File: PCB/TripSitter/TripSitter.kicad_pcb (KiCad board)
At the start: 4 copper layers, 203 x 85 mm, 165 parts, among them IC1 MT25QL256ABA1EW9-0SIT, IC701 IP4220CZ6, J2 DE15_Plug_HighDensity_Mountin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, J201 Conn_ARM_JTAG_SWD_20, J3 USB_B_Micro, J4 Conn_02x07_Odd_Even, J6 EFM32_PinHeader_PortE, J7 HDMI_A_1.4, J801 Conn_02x05_Odd_Even, J802 Jack-DC, J803 USB_B_Micro, SW1 SW_Push_Open, SW801 SW_DPDT_x2, U1 XC7A100T-FGG484, U2 TPS54325_PWP_14, U201 EFM32GG11B420F2048GQ100, U202 IS62WVS2568FBLL-20NLI, U4 DSC1001DL5-100.0000T, U5 TPS54294PWP, U501 IS62WVS2568FBLL-20NLI, U502 IS62WVS2568FBLL-20NLI, U6 IS62WVS2568FBLL-20NLI, U7 TPD12S520DBT, Y201 48MHz

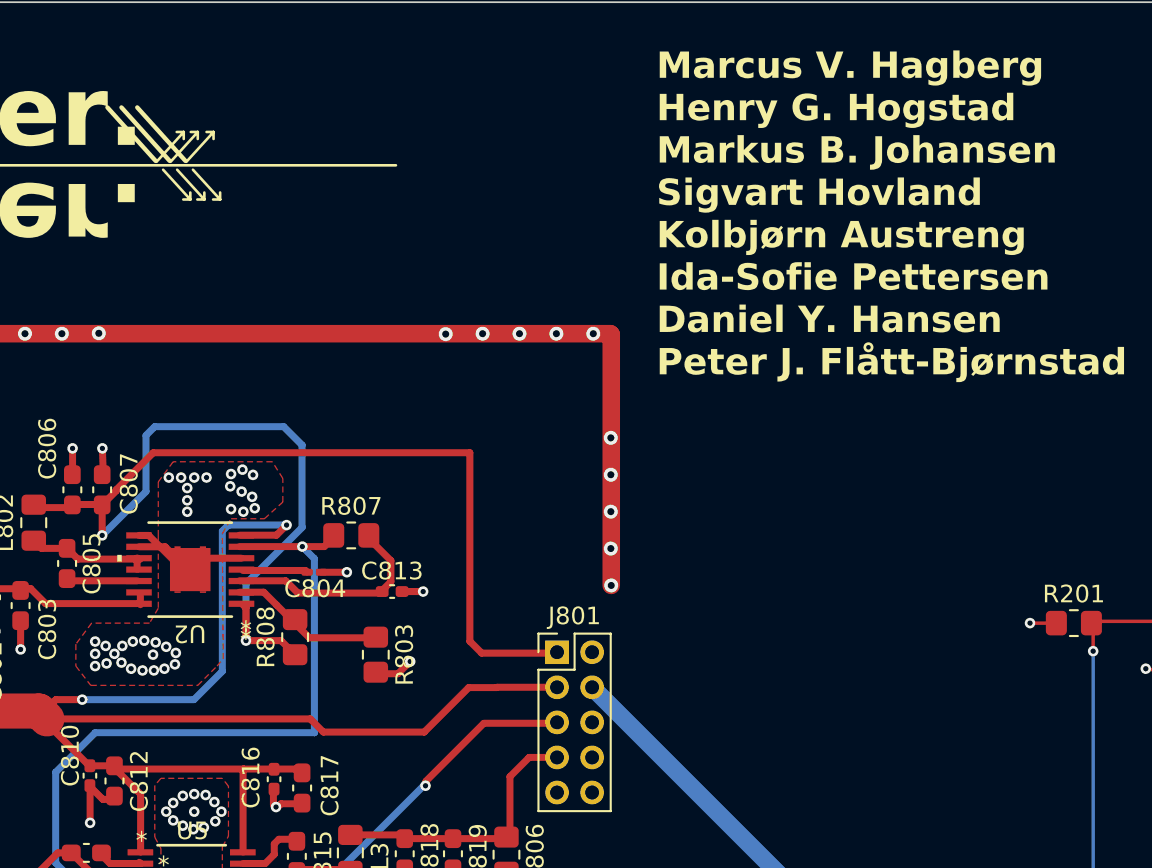
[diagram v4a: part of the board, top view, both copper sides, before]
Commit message: Fix 3V3 power level to be more open and delete unused backups (#19)
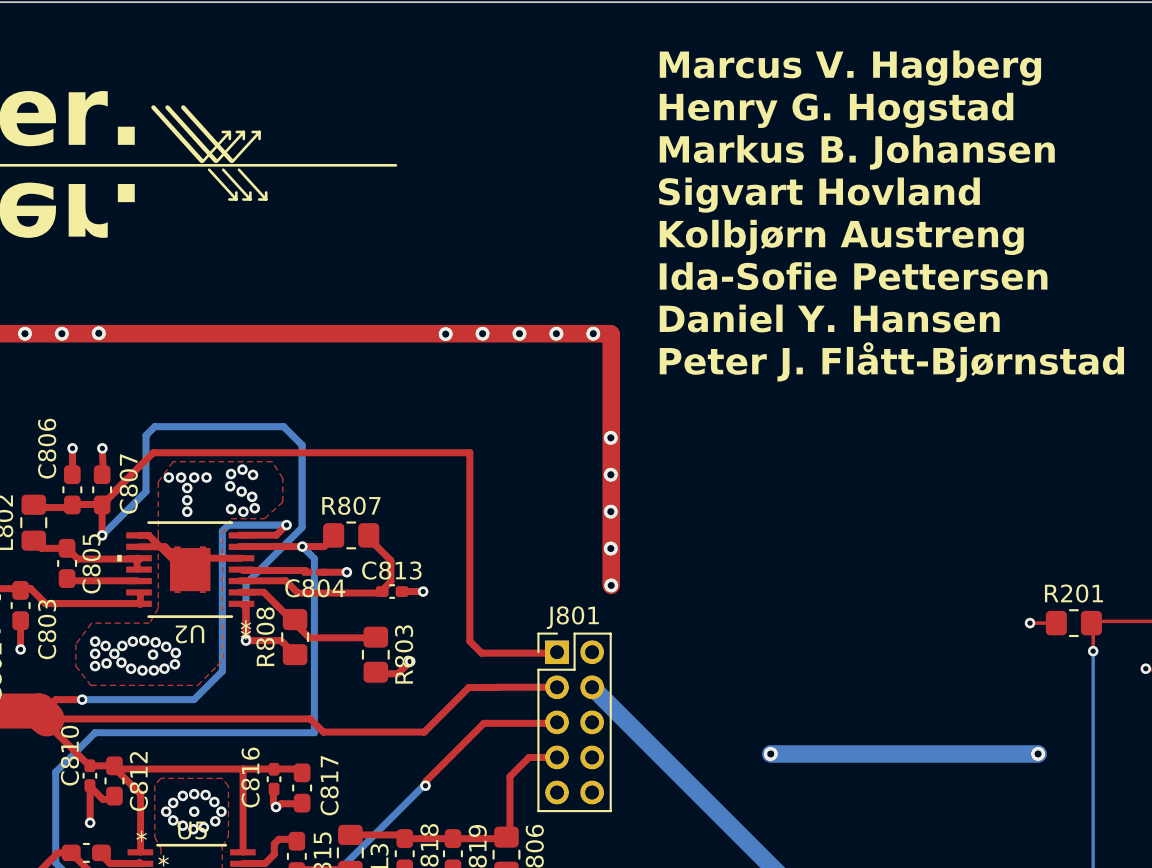
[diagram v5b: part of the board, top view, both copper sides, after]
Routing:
- net +1V8: track 125.1 -> 126.1 mm, vias 10 -> 12

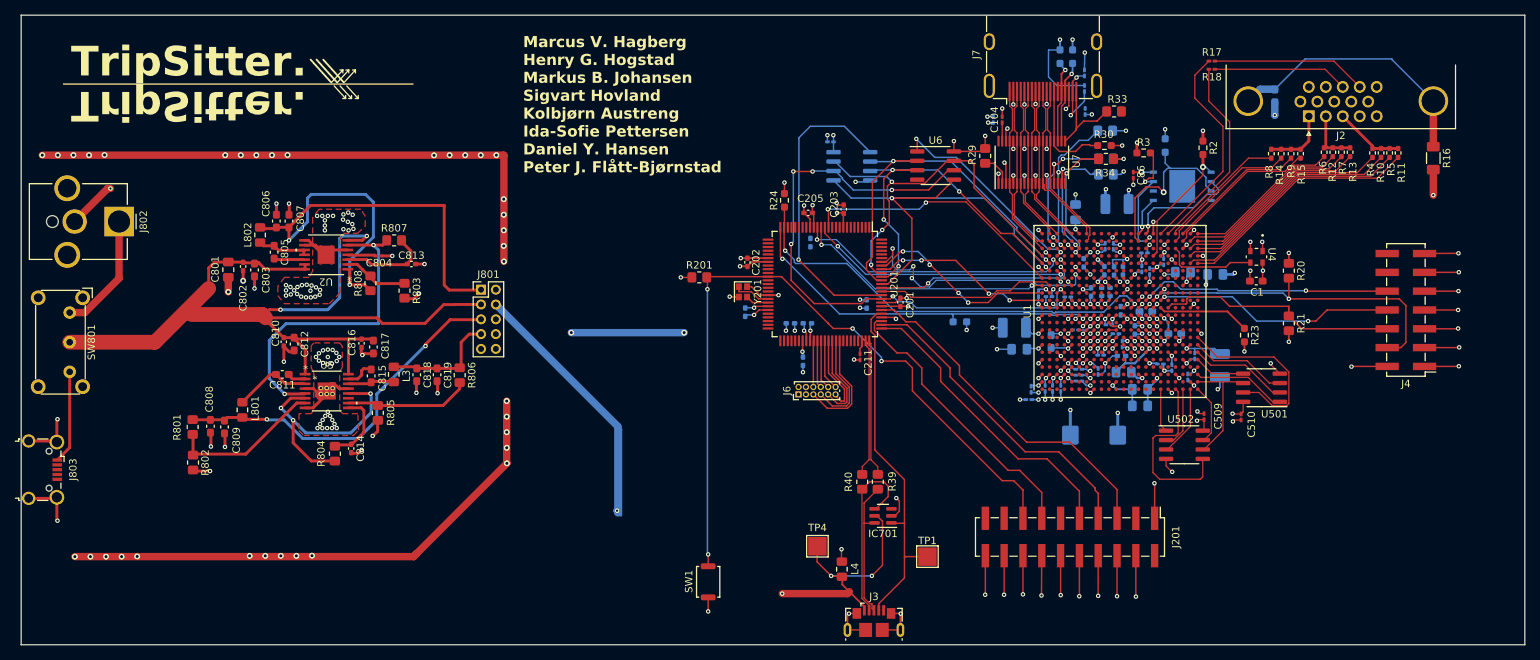
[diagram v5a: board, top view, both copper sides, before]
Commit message: pcb: fix unconnected items
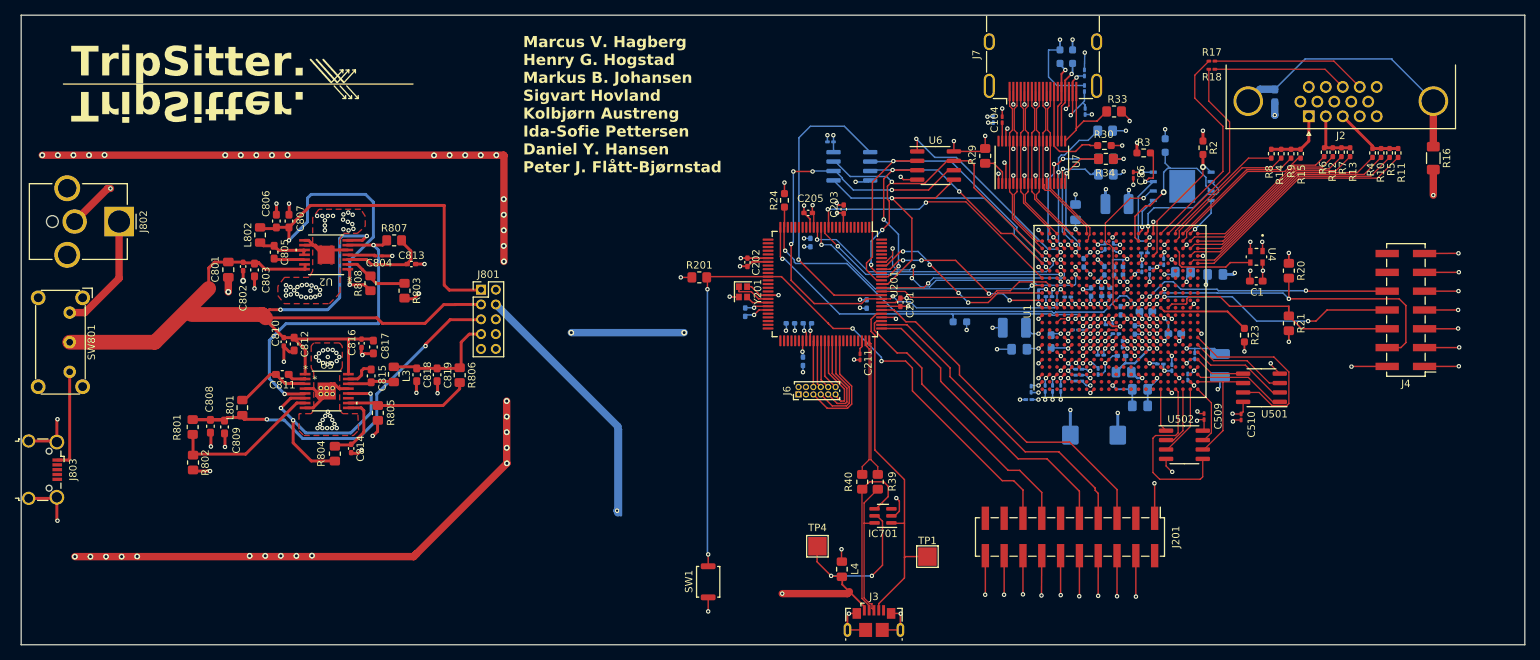
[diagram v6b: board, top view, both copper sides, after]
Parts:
- moved L801 0.30 mm to (52.1, 71.1)
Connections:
- U1 pad C15: MCU_PE8 -> unconnected-(U1B-IO_L3N_T0_DQS_16-PadC15)
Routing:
- net Net-(IC1-C): track 0.00 -> 20.5 mm, vias 0 -> 1
- net GND: track 542.5 -> 554.9 mm, vias 279 -> 282
- net /PCB Power System/1V8: track 49.1 -> 53.5 mm
- net +1V8: track 126.1 -> 129.9 mm
- net +5V: track 268.5 -> 270.8 mm
- net /FPGA Artix-7 100T 1FGG484C/Programmer interface/QSPI_DQ2: track 24.5 -> 22.5 mm
- net +3.3V: track 134.4 -> 135.2 mm, vias 63 -> 64

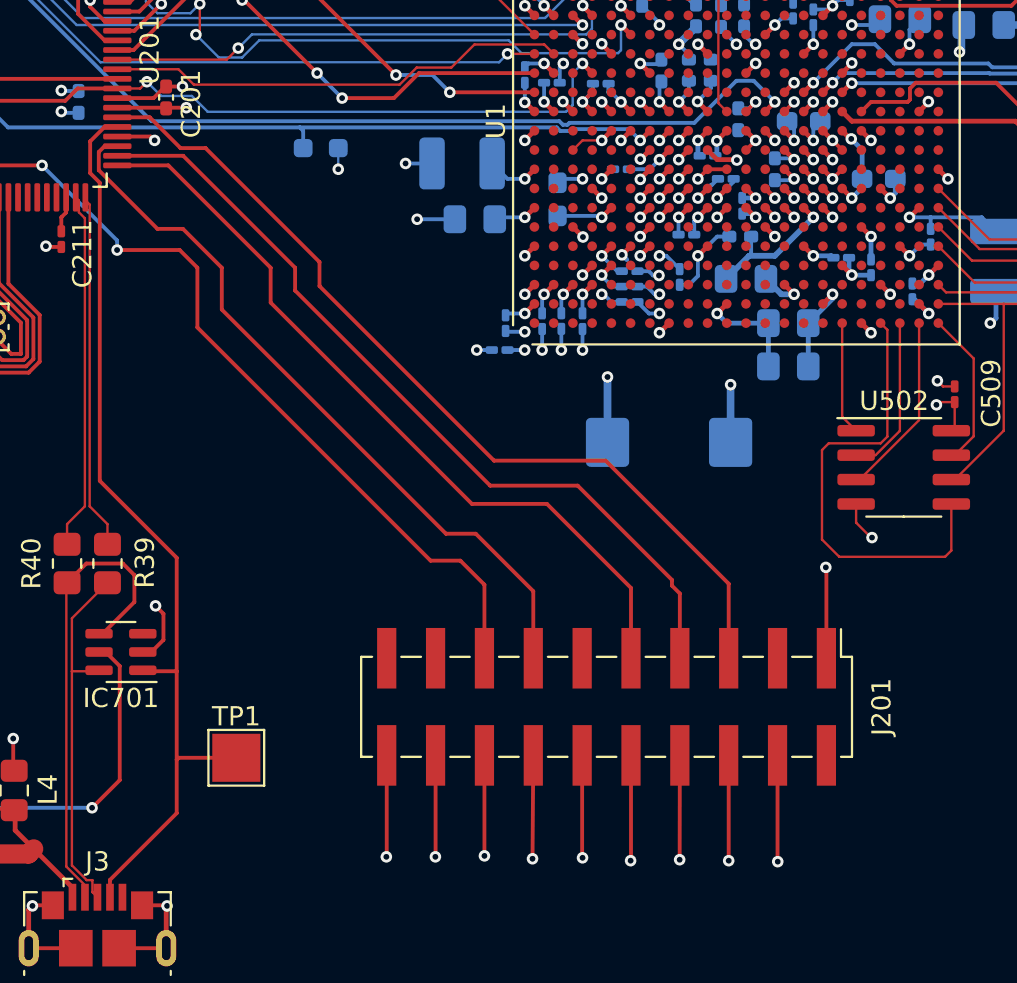
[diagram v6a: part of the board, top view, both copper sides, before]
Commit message: edit jtag debug connector
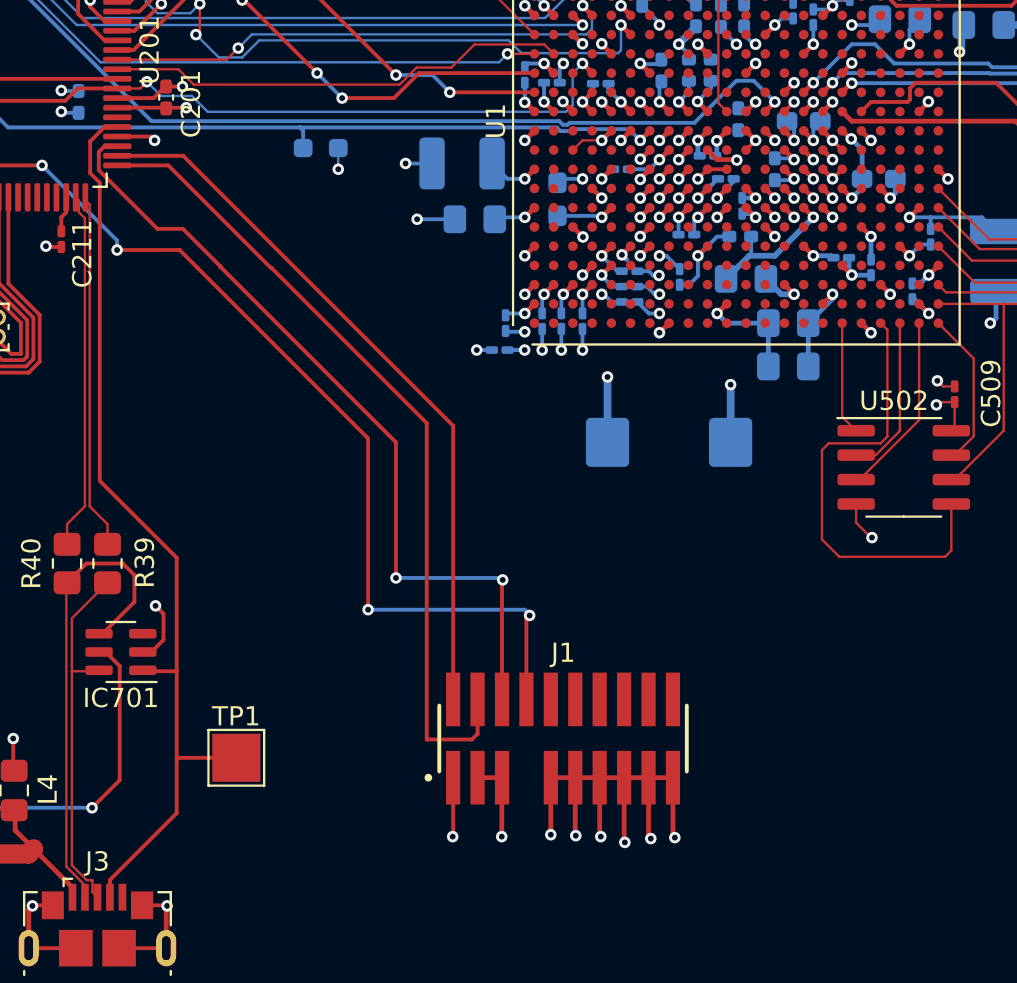
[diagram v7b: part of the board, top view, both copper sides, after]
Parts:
- removed J201: Conn_ARM_JTAG_SWD_20, Connector_PinHeader_2.54mm:PinHeader_2x10_P2.54mm_Vertical_SMD
- added J1: FTSH-110-01-L-DV-007, FTSH-110-01-L-DV-007:SAMTEC_FTSH-110-01-L-DV-007, F.Cu at (161.6, 90.2)
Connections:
- U1 pad C15: unconnected-(U1B-IO_L3N_T0_DQS_16-PadC15) -> MCU_PE8
- U201 pad 81: Net-(J201-TDI) -> unconnected-(U201C-PF5-Pad81)
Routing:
- net Net-(J201-TDI): track 46.4 -> 0.00 mm
- net GND: track 554.9 -> 536.0 mm, vias 282 -> 280
- net EFM32_RESETN: track 99.7 -> 106.8 mm, vias 4 -> 6
- net Net-(U201C-PF1): track 42.9 -> 37.5 mm
- net +3.3V: track 135.2 -> 130.4 mm, vias 64 -> 63
- net Net-(U201C-PF2): track 38.5 -> 42.5 mm, vias 0 -> 2
- net +3V3: track 0.00 -> 3.14 mm, vias 0 -> 1
- net Net-(U201C-PF0): track 40.5 -> 42.6 mm
